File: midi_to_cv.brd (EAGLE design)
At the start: 100 x 80 mm, 32 parts, among them IC1 TL084P, U1 ATMEGA328P_PDIP

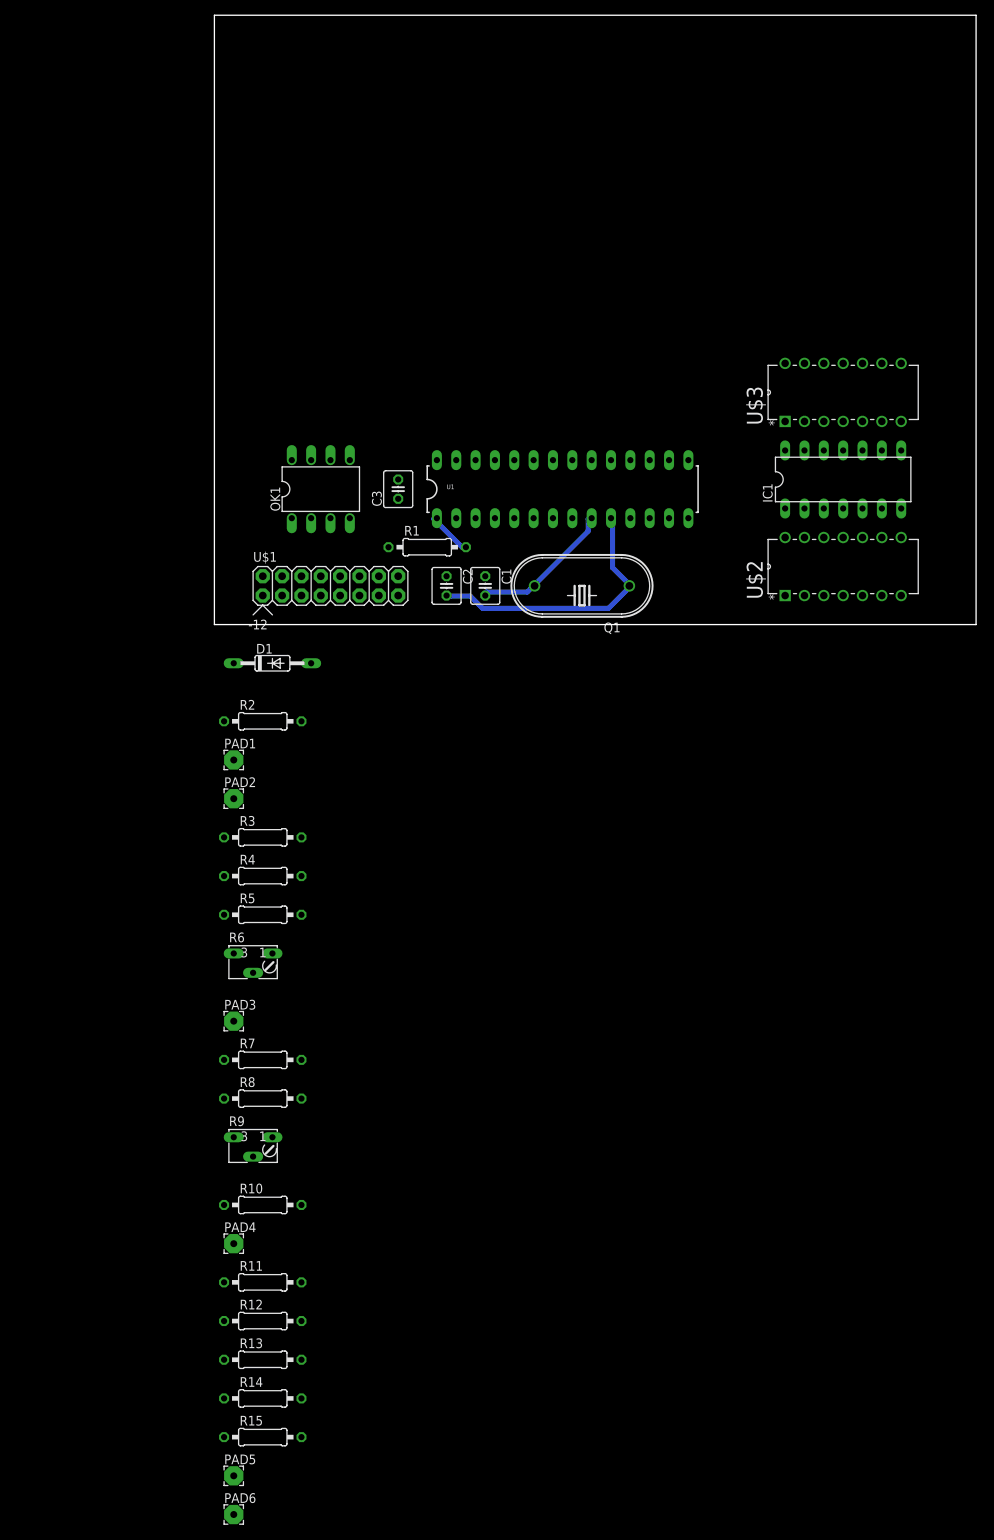
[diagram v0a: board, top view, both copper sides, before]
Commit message: converting to 4822
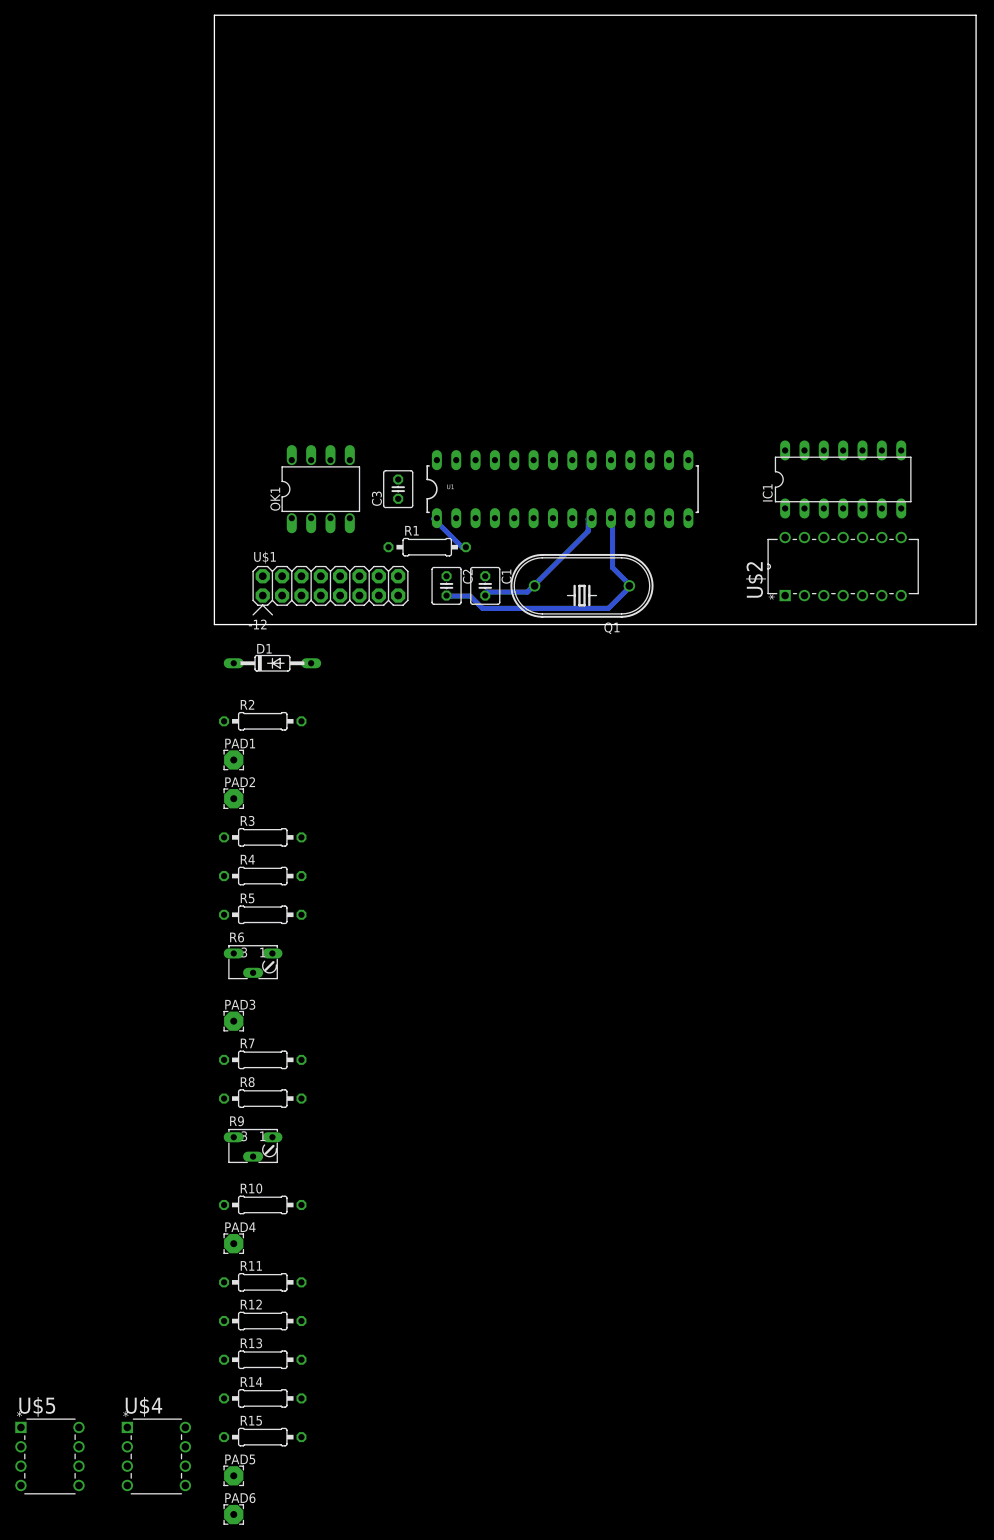
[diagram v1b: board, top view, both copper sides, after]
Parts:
- removed U$3: MCP4922-E/P, MCP4922:DIP254P762X533-14
- added U$4, U$5: MCP4822-E/P, MCP4822:DIP254P762X432-8
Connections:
- new net N$30: OK1.6, R3.1
- new net VDD: U$5.1
- net +5V: now also U$4.1; no longer U$3.1, U$3.11, U$3.13
- net GND: now also U$4.5, U$4.7; no longer U$3.12, U$3.8
- net N$10: no longer OK1.6, R3.1
- net N$14: now also U$4.6; no longer U$3.10
- net N$2: now also U$4.8; no longer U$3.14
- net N$25: now also U$4.3; no longer U$3.4
- net N$26: now also U$4.4; no longer U$3.5
- net N$27: now also U$4.2; no longer U$3.3

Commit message: converted to 4822
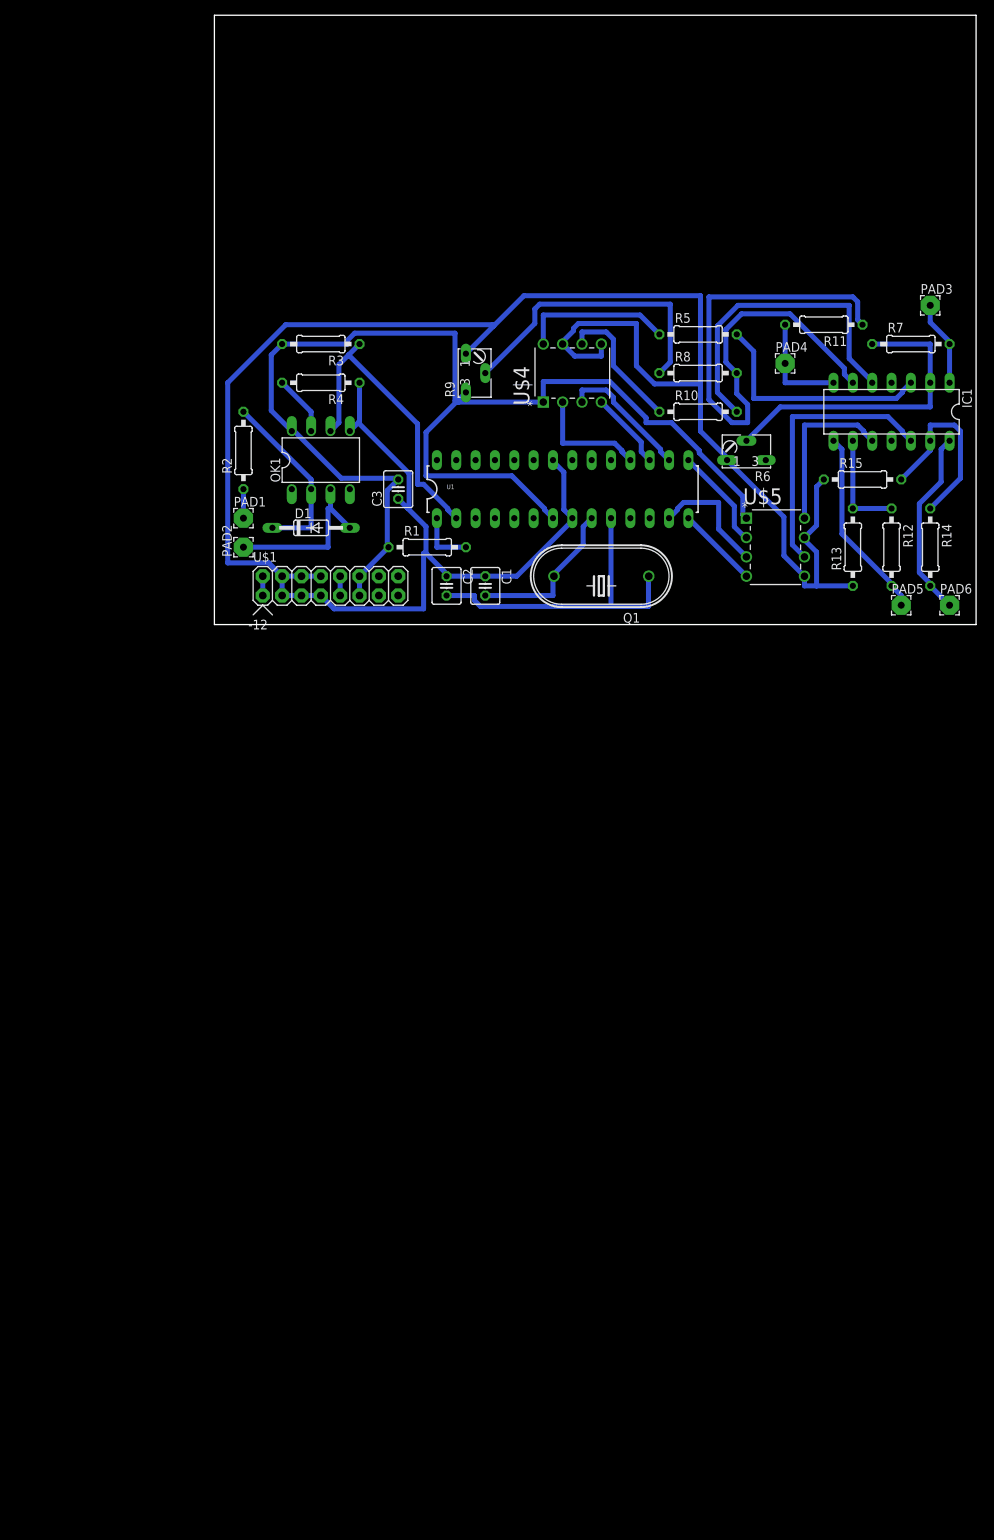
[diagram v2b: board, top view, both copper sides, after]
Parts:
- removed U$2: MCP4922-E/P, MCP4922:DIP254P762X533-14
- moved U$4 159.5 mm to (50.8, 36.8), turned to 90 degrees
- moved U$5 152.7 mm to (77.5, 6.35)
- moved PAD6 151.9 mm to (96.5, 2.54)
- moved R15 148.4 mm to (85.1, 19.1)
- moved R11 145.7 mm to (80.0, 39.4), turned to 180 degrees
- moved PAD5 144.0 mm to (90.2, 2.54)
- moved R14 142.0 mm to (94.0, 10.2), turned to 270 degrees
- moved PAD4 136.4 mm to (74.9, 34.3)
- moved R13 131.8 mm to (83.8, 10.2), turned to 90 degrees
- moved PAD3 131.1 mm to (94.0, 41.9)
- moved R12 130.9 mm to (88.9, 10.2), turned to 270 degrees
- moved R7 126.8 mm to (91.4, 36.8)
- moved R10 118.8 mm to (63.5, 27.9)
- moved R8 111.1 mm to (63.5, 33.0)
- moved R9 104.1 mm to (33.0, 33.0), turned to 90 degrees
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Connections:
- removed net N$10: U1.2
- removed net VDD: U$5.1
- net +5V: now also U$5.1; no longer U$2.1, U$2.11, U$2.13
- net GND: now also U$5.5, U$5.7; no longer U$2.12, U$2.8
- net N$18: now also U$5.8; no longer U$2.14
- net N$23: now also U$5.4; no longer U$2.5
- net N$24: now also U$5.6; no longer U$2.10
- net N$28: now also U$5.3; no longer U$2.4
- net N$29: now also U$5.2; no longer U$2.3
- net N$30: now also U1.2
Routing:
- net GND: track 0.00 -> 299.7 mm
- net +5V: track 0.00 -> 162.2 mm
- net N$13: track 0.00 -> 78.0 mm
- net N$15: track 0.00 -> 42.2 mm
- net N$12: track 0.00 -> 41.8 mm
- net N$30: track 0.00 -> 40.8 mm
- net N$16: track 0.00 -> 38.8 mm
- net N$24: track 0.00 -> 36.0 mm
- net N$6: track 0.00 -> 30.9 mm
- net N$19: track 0.00 -> 25.3 mm
- net N$21: track 0.00 -> 24.9 mm
- net N$22: track 0.00 -> 24.8 mm
- net N$7: track 0.00 -> 24.0 mm
- net N$3: track 0.00 -> 22.6 mm
- net N$18: track 0.00 -> 22.1 mm
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
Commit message: remembering the gate output
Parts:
- added PAD7: gate output, wirepad:2,54/0,9
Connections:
- new net N$10: PAD7.1, U1.19
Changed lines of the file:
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@@
 <attribute name="OC_FARNELL" value="1439413" x="77.47" y="6.35" size="1.778" layer="27" display="off"/>
 </element>
+<element name="PAD7" library="wirepad" package="2,54/0,9" value="gate output" x="2.54" y="-5.08"/>
 </elements>
 <signals>
@@
 <wire x1="77.47" y1="13.97" x2="77.47" y2="26.19375" width="0.6604" layer="16"/>
 </signal>
+<signal name="N$10">
+<contactref element="U1" pad="19"/>
+<contactref element="PAD7" pad="1"/>
+<wire x1="2.54" y1="-5.08" x2="52.07" y2="21.59" width="0" layer="19" extent="1-1"/>
+</signal>
 </signals>
